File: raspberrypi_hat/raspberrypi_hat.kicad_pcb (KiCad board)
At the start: 4 copper layers, 65 x 56 mm, 18 parts, among them J3 40HAT, J6 CONN_02X02, J9 CONN_01X02, Q1 DMG2305UX, Q2 DMMT5401, U2 CAT24C32

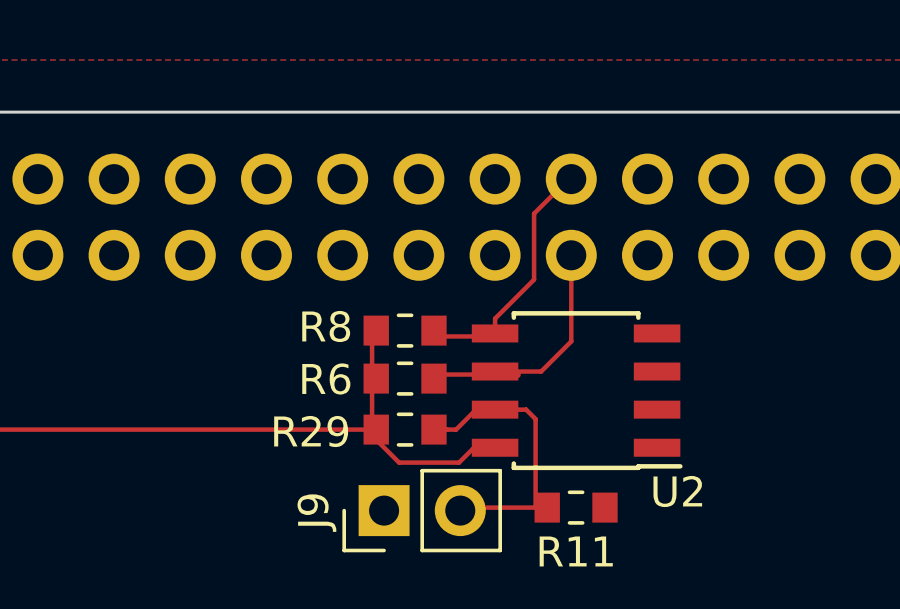
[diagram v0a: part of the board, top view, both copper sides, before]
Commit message: Fix incorrect SDA and SCL pin on Raspberry pi hat EEPROM
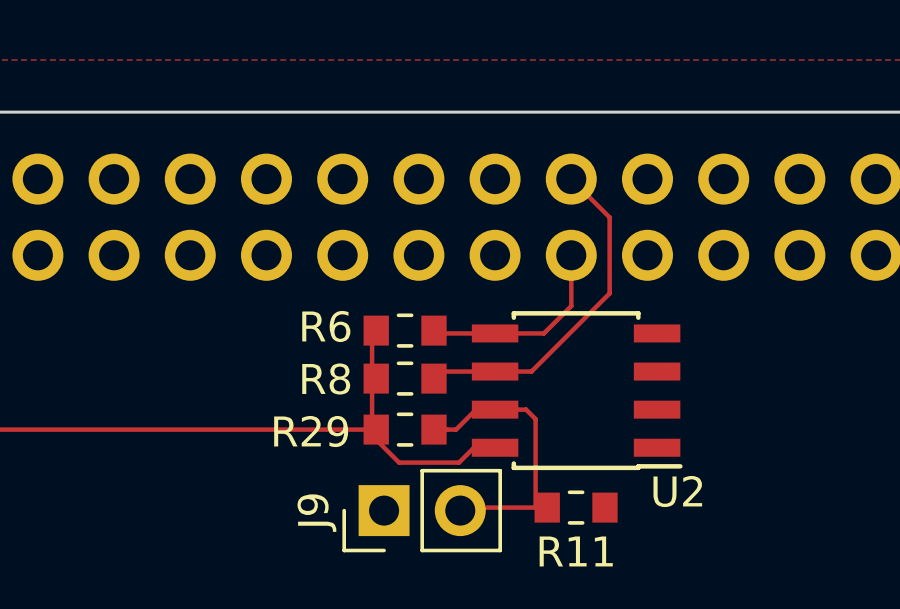
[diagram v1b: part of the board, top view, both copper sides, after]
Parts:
- removed the R8 at (114.4, 68.1)
- added R6: 3.9K, Resistor_SMD:R_0603_1608Metric_Pad0.84x1.00mm_HandSolder, F.Cu at (114.4, 68.1)
- R23: value 22 -> 10K
- R24: value 22 -> 47K
- renumbered R6 to R8
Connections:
- J3 pad 10: Net-(J3-Pad10) -> (no net)
- J3 pad 11: Net-(J3-Pad11) -> (no net)
- J3 pad 12: Net-(J3-Pad12) -> (no net)
- J3 pad 13: Net-(J3-Pad13) -> (no net)
- J3 pad 15: Net-(J3-Pad15) -> (no net)
- J3 pad 16: Net-(J3-Pad16) -> (no net)
- J3 pad 17: Net-(J3-Pad17) -> (no net)
- J3 pad 18: Net-(J3-Pad18) -> (no net)
- J3 pad 19: Net-(J3-Pad19) -> (no net)
- J3 pad 21: Net-(J3-Pad21) -> (no net)
- J3 pad 22: Net-(J3-Pad22) -> (no net)
- J3 pad 23: Net-(J3-Pad23) -> (no net)
- J3 pad 24: Net-(J3-Pad24) -> (no net)
- J3 pad 26: Net-(J3-Pad26) -> (no net)
- J3 pad 29: Net-(J3-Pad29) -> (no net)
- J3 pad 3: Net-(J3-Pad3) -> (no net)
- J3 pad 31: Net-(J3-Pad31) -> (no net)
- J3 pad 32: Net-(J3-Pad32) -> (no net)
- J3 pad 33: Net-(J3-Pad33) -> (no net)
- J3 pad 35: Net-(J3-Pad35) -> (no net)
- J3 pad 36: Net-(J3-Pad36) -> (no net)
- J3 pad 37: Net-(J3-Pad37) -> (no net)
- J3 pad 38: Net-(J3-Pad38) -> (no net)
- J3 pad 40: Net-(J3-Pad40) -> (no net)
- J3 pad 5: Net-(J3-Pad5) -> (no net)
- J3 pad 7: Net-(J3-Pad7) -> (no net)
- J3 pad 8: Net-(J3-Pad8) -> (no net)
- R8 pad 2: /ID_SD_EEPROM -> /ID_SC_EEPROM
- U2 pad 5: /ID_SC_EEPROM -> /ID_SD_EEPROM
- U2 pad 6: /ID_SD_EEPROM -> /ID_SC_EEPROM
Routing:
- net /ID_SC_EEPROM: track 8.17 -> 11.7 mm
- net /ID_SD_EEPROM: track 8.99 -> 7.43 mm
